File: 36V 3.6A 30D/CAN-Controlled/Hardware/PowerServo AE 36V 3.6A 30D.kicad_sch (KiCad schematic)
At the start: 27 parts, among them IC1 DRV8251DDAR, J1 Control_In, J2 MOT_A, J3 Prog_IN, J4 Power_In, J6 Control_In, J7 MOT_B, U1 LMZM23601V5, U2 TLV76733DRVx, U4 MA730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

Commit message: Flow
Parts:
- added J5: Power_In, Connector_AMASS:AMASS_XT30UPB-M_1x02_P5.0mm_Vertical, symbol Connector_Generic:Conn_01x02
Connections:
- net +12V: now also J5.2 (Pin_2)
- net GND: now also J5.1 (Pin_1)
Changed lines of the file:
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@@
+	)
+	(junction
+		(at 106.68 83.82)
+		(diameter 0)
+		(color 0 0 0 0)
 	)
 	(junction
@@
 	)
 	(junction
+		(at 106.68 86.36)
+		(diameter 0)
+		(color 0 0 0 0)
+	)
+	(junction
 		(at 110.49 151.13)
 		(diameter 0)
@@
 	(wire
 		(pts
+			(xy 99.06 86.36) (xy 99.06 90.17)
+		)
+		(stroke
+			(width 0)
+			(type default)
+		)
+	)
+	(wire
+		(pts
 			(xy 114.3 83.82) (xy 130.81 83.82)
 		)
@@
 	(wire
 		(pts
-			(xy 106.68 86.36) (xy 107.95 86.36)
+			(xy 106.68 86.36) (xy 109.22 86.36)
 		)
 		(stroke
@@
 	(wire
 		(pts
+			(xy 106.68 80.01) (xy 106.68 83.82)
+		)
+		(stroke
+			(width 0)
+			(type default)
+		)
+	)
+	(wire
+		(pts
 			(xy 109.22 83.82) (xy 114.3 83.82)
 		)
@@
 	(wire
 		(pts
+			(xy 99.06 90.17) (xy 106.68 90.17)
+		)
+		(stroke
+			(width 0)
+			(type default)
+		)
+	)
+	(wire
+		(pts
 			(xy 223.52 133.35) (xy 229.87 133.35)
 		)
@@
 	(wire
 		(pts
+			(xy 106.68 90.17) (xy 106.68 86.36)
+		)
+		(stroke
+			(width 0)
+			(type default)
+		)
+	)
+	(wire
+		(pts
 			(xy 247.65 127) (xy 257.81 127)
 		)
@@
 	(wire
 		(pts
+			(xy 99.06 83.82) (xy 99.06 80.01)
+		)
+		(stroke
+			(width 0)
+			(type default)
+		)
+	)
+	(wire
+		(pts
 			(xy 115.57 124.46) (xy 109.22 124.46)
+		)
+		(stroke
+			(width 0)
+			(type default)
+		)
+	)
+	(wire
+		(pts
+			(xy 99.06 80.01) (xy 106.68 80.01)
 		)
 		(stroke
@@
 	(symbol
 		(lib_id "power:GND")
-		(at 107.95 86.36 0)
+		(at 109.22 86.36 0)
 		(unit 1)
 		(exclude_from_sim no)
@@
 		(fields_autoplaced yes)
 		(property "Reference" "#PWR07"
-			(at 107.95 92.71 0)
+			(at 109.22 92.71 0)
 			(effects
 				(font
@@
 		)
 		(property "Value" "GND"
-			(at 107.95 91.44 0)
+			(at 109.22 91.44 0)
 			(effects
 				(font
@@
 		)
 		(property "Footprint" ""
-			(at 107.95 86.36 0)
+			(at 109.22 86.36 0)
 			(effects
 				(font
@@
 		)
 		(property "Datasheet" ""
-			(at 107.95 86.36 0)
+			(at 109.22 86.36 0)
 			(effects
 				(font
@@
 		)
 		(property "Description" "Power symbol creates a global label with name \"GND\" , ground"
-			(at 107.95 86.36 0)
+			(at 109.22 86.36 0)
 			(effects
 				(font
@@
 					(unit 1)
 				)
+			)
+		)
+	)
+	(symbol
+		(lib_id "Connector_Generic:Conn_01x02")
+		(at 93.98 86.36 180)
+		(unit 1)
+		(exclude_from_sim no)
+		(in_bom yes)
+		(on_board yes)
+		(dnp no)
+		(fields_autoplaced yes)
+		(property "Reference" "J5"
+			(at 93.98 77.47 0)
+			(effects
+				(font
+					(size 1.27 1.27)
+				)
+			)
+		)
+		(property "Value" "Power_In"
+			(at 93.98 80.01 0)
+			(effects
+				(font
+					(size 1.27 1.27)
+				)
+			)
+		)
+		(property "Footprint" "Connector_AMASS:AMASS_XT30UPB-M_1x02_P5.0mm_Vertical"
+			(at 93.98 86.36 0)
+			(effects
+				(font
+					(size 1.27 1.27)
+				)
+				(hide yes)
+			)
+		)
+		(property "Datasheet" "~"
+			(at 93.98 86.36 0)
+			(effects
+				(font
+					(size 1.27 1.27)
+				)
+				(hide yes)
+			)
+		)
+		(property "Description" "Generic connector, single row, 01x02, script generated (kicad-library-utils/schlib/autogen/connector/)"
+			(at 93.98 86.36 0)
+			(effects
+				(font
+					(size 1.27 1.27)
+				)
+				(hide yes)
+			)
+		)
+		(pin "1"
+		)
+		(pin "2"
+		)
+		(instances
+			(project "PowerServo AE 36V 3.6A 30D"
+				(path "/9917aed5-eb52-468d-8a21-f8d37f4ad995"
+					(reference "J5")
+					(unit 1)
+				)

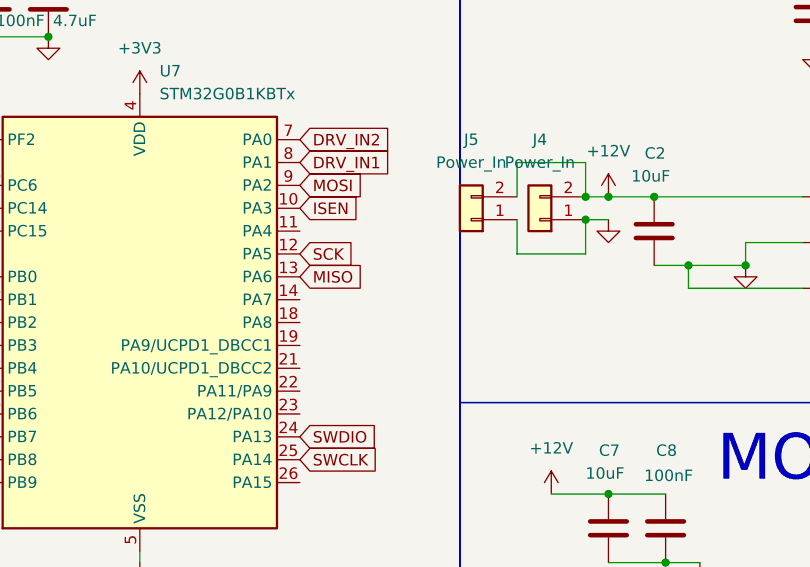
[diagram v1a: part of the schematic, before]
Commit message: Flowchart update. PCB Update to include 2nd XT30
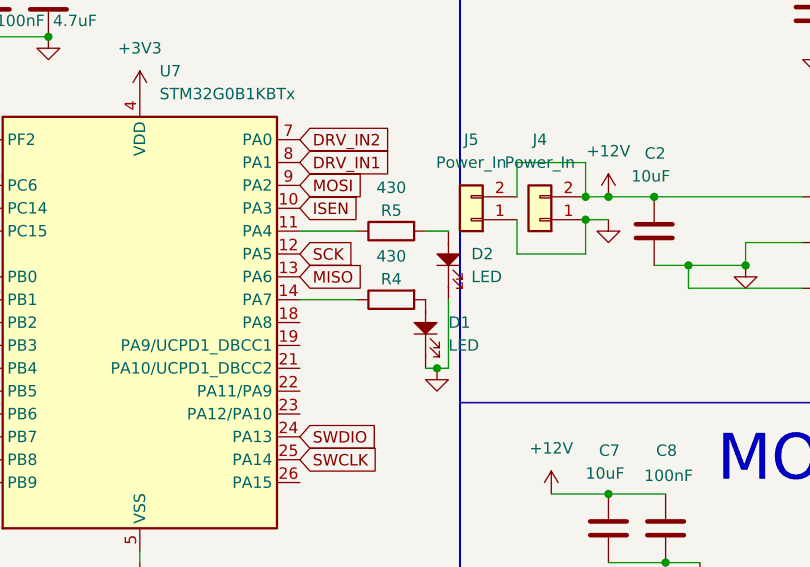
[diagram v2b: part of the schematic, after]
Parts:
- added D1, D2: LED, LED_SMD:LED_0402_1005Metric, symbol PCM_SL_Devices:LED
- added R4, R5: 430, Resistor_SMD:R_0402_1005Metric, symbol Device:R
- IC1: footprint SOIC127P600X170-9N -> _custom:SOIC127P600X170-9N
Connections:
- net GND: now also D1.1, D2.1
- net at U7.11 (PA4): now also R5.1
- net at U7.14 (PA7): now also R4.1
- new net: D2.2, R5.2
- new net: D1.2, R4.2
